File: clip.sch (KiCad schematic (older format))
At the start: 47 parts, among them J1 LiPo, J2 USB_B_Micro, J3 BME680, J4 LIS3DH, J5 Conn_01x07, J6 Conn_01x18, J7 Conn_01x18, Q1 2.5A/30V, Q2 S8050, Q3 S8050, SW1 Switch, SW2 Switch, U1 MCP73831, U2 AP2112K-3.3, U3 FT231XS, U4 ESP32-WROOM-32

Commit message: Rename project
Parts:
- J2: symbol Connector:USB_B_Micro -> clip-rescue:USB_B_Micro-Connector-clip_20200407-rescue
- U2: symbol Regulator_Linear:AP2112K-3.3 -> clip-rescue:AP2112K-3.3-Regulator_Linear-clip_20200407-rescue
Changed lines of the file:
@@
 3.3V
 $Comp
-L Regulator_Linear:AP2112K-3.3 U2
+L clip-rescue:AP2112K-3.3-Regulator_Linear-clip_20200407-rescue U2
 U 1 1 5E773568
 P 2850 1700
@@
 $EndComp
 $Comp
-L Connector:USB_B_Micro J2
+L clip-rescue:USB_B_Micro-Connector-clip_20200407-rescue J2
 U 1 1 5E93C6CC
 P 8000 1800
@@
 Data
 89 50 4E 47 0D 0A 1A 0A 00 00 00 0D 49 48 44 52 00 00 02 EE 00 00 02 1A 08 02 00 00 00 F0 7C 5F
-92 00 00 00 03 73 42 49 54 08 08 08 DB E1 4F E0 00 00 00 09 70 48 59 73 00 00 0E C3 00 00 0E C3
-01 C7 6F A8 64 00 00 20 00 49 44 41 54 78 9C EC BD 77 B4 25 55 99 36 FE BC EF DE BB C2 39 E7 A6
+92 00 00 00 03 73 42 49 54 08 08 08 DB E1 4F E0 00 00 00 09 70 48 59 73 00 00 0E 74 00 00 0E 74
+01 6B 24 B3 D6 00 00 20 00 49 44 41 54 78 9C EC BD 77 B4 25 55 99 36 FE BC EF DE BB C2 39 E7 A6
 EE DB 89 D0 82 C0 88 62 40 07 14 01 85 31 A1 A0 32 E6 08 06 18 31 8E A2 A3 9F A3 A3 23 26 C4 30
 62 D6 31 A0 98 C5 88 A2 A8 33 62 18 B3 62 FA 50 04 15 41 E8 6E BA A1 FB 86 13 AA 6A EF FD BE DF

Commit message: Update design
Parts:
- removed D4: Green, LED_SMD:LED_0805_2012Metric_Pad1.15x1.40mm_HandSolder, symbol Device:LED
- removed J5: Conn_01x07, Connector_PinHeader_2.54mm:PinHeader_1x07_P2.54mm_Vertical, symbol Connector_Generic:Conn_01x07
- removed J6, J7: Conn_01x18, Connector_PinHeader_2.54mm:PinHeader_1x18_P2.54mm_Vertical, symbol Connector_Generic:Conn_01x18
- removed R3: 1K, Resistor_SMD:R_0805_2012Metric_Pad1.15x1.40mm_HandSolder, symbol Device:R_US
- D1: value Red -> Green
- J2: footprint Connector_USB:USB_Micro-B_Amphenol_10103594-0001LF_Horizontal -> Connector_USB:USB_Micro-B_Wuerth_614105150721_Vertical; Digikey 609-4050-1-ND -> 732-5958-1-ND; Digikey_link https://www.digikey.de/product-detail/en/amphenol-icc-fci/1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 -> https://www.digikey.de/product-detail/en/w%C3%BCrth-elektro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; Manufacturer 10103594-0001LF -> 614105150721
- J3: Digikey S7045-ND -> S7006-ND; Digikey_link https://www.digikey.de/product-detail/en/sullins-connector-solutions/PPPC121LFBN-RC/S7045-ND/810184 -> https://www.digikey.de/product-detail/en/sullins-connector-solutions/PPTC081LFBN-RC/S7006-ND/810147; Manufacturer PPPC121LFBN-RC -> PPTC081LFBN-RC
- J4: Digikey 732-5321-ND -> S7006-ND; Digikey_link https://www.digikey.de/product-detail/en/w%C3%BCrth-elektro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 -> https://www.digikey.de/product-detail/en/sullins-connector-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; Manufacturer 61300811121 -> PPTC081LFBN-RC
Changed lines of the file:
@@
 Text Notes 7700 4300 0    39   ~ 0
 Reference: SparkFun_ESP32_thing
-Wire Notes Line
-	4650 550  500  550
 Text Notes 600  650  0    50   ~ 0
 Voltage Regulator and Battery
@@
 Wire Notes Line
 	4700 550  7600 550
-Text Notes 4750 2500 0    39   ~ 0
-Reference: SparkFun_ESP32_Thing_Plus\nCharge current:\nI_CHG = 1000 / R_PROG\nR_PROG=2K : I_CHG=500mA
 Text Notes 4750 650  0    50   ~ 0
 Lithium-Polymer Battery Charger (1-cell)
@@
 P 5800 1050
 F 0 "D1" V 5850 1150 50  0000 L CNN
-F 1 "Red" V 5750 1150 50  0000 L CNN
+F 1 "Green" V 5750 1150 50  0000 L CNN
 F 2 "LED_SMD:LED_0805_2012Metric_Pad1.15x1.40mm_HandSolder" H 5800 1050 50  0001 C CNN
 F 3 "https://katalog.we-online.de/led/datasheet/150080RS75000.pdf" H 5800 1050 50  0001 C CNN
@@
 IO35
 $Comp
-L Connector_Generic:Conn_01x18 J6
+L Connector_Generic:Conn_01x18 #J6
 U 1 1 5E81200B
 P 4150 6400
-F 0 "J6" H 4068 7325 50  0000 C CNN
+F 0 "#J6" H 4068 7325 50  0000 C CNN
 F 1 "Conn_01x18" H 4068 7326 50  0001 C CNN
 F 2 "Connector_PinHeader_2.54mm:PinHeader_1x18_P2.54mm_Vertical" H 4150 6400 50  0001 C CNN
@@
 	5400 5600 5500 5600
 $Comp
-L Connector_Generic:Conn_01x18 J7
+L Connector_Generic:Conn_01x18 #J7
 U 1 1 5E8DE4F0
 P 5200 6400
-F 0 "J7" H 5118 7325 50  0000 C CNN
+F 0 "#J7" H 5118 7325 50  0000 C CNN
 F 1 "Conn_01x18" H 5118 7326 50  0001 C CNN
 F 2 "Connector_PinHeader_2.54mm:PinHeader_1x18_P2.54mm_Vertical" H 5200 6400 50  0001 C CNN
@@
 Reference: NodeMCU_ESP32
 $Comp
-L Device:LED D4
+L Device:LED #D4
 U 1 1 5E75A88B
 P 6050 1950
-F 0 "D4" V 6100 2050 50  0000 L CNN
-F 1 "Green" V 6000 2050 50  0000 L CNN
+F 0 "#D4" V 6100 2050 50  0000 L CNN
+F 1 "Red" V 6000 2050 50  0000 L CNN
 F 2 "LED_SMD:LED_0805_2012Metric_Pad1.15x1.40mm_HandSolder" H 6050 1950 50  0001 C CNN
 F 3 "https://katalog.we-online.de/led/datasheet/150080GS75000.pdf" H 6050 1950 50  0001 C CNN
@@
 $EndComp
 $Comp
-L Device:R_US R3
+L Device:R_US #R3
 U 1 1 5E759248
 P 6050 1650
-F 0 "R3" H 5850 1600 50  0000 L CNN
+F 0 "#R3" H 5850 1600 50  0000 L CNN
 F 1 "1K" H 5900 1700 50  0000 L CNN
 F 2 "Resistor_SMD:R_0805_2012Metric_Pad1.15x1.40mm_HandSolder" V 6090 1640 50  0001 C CNN
@@
 	10500 5200 10850 5200
 $Comp
-L Connector_Generic:Conn_01x07 J5
+L Connector_Generic:Conn_01x07 #J5
 U 1 1 5E79B981
 P 6250 5900
-F 0 "J5" H 6330 5942 50  0000 L CNN
+F 0 "#J5" H 6330 5942 50  0000 L CNN
 F 1 "Conn_01x07" H 6330 5851 50  0001 L CNN
 F 2 "Connector_PinHeader_2.54mm:PinHeader_1x07_P2.54mm_Vertical" H 6250 5900 50  0001 C CNN
@@
 	1    0    0    -1
 $EndComp
-Text Notes 2700 1250 0    39   ~ 0
+Text Notes 2500 1250 0    39   ~ 0
 AP2112K/AMS1117-3.3\n
 Text Notes 1500 1150 0    39   ~ 0
@@
 Text Notes 850  1900 0    39   ~ 0
 BAT20J/S4-1N5819/SS14\n
-Text Notes 600  2500 0    39   ~ 0
-Reference: SparkFun_ESP32_Thing_Plus\nVBUS - 6V MAX\nBATT - Single Cell (4.2V MAX)
 Wire Wire Line
 	1850 1600 2300 1600
@@
 Wire Wire Line
 	8700 3100 8700 3000
-Connection ~ 8700 3100
 Wire Wire Line
 	8450 3100 8700 3100
-Wire Wire Line
-	8450 3150 8450 3100
-$Comp
-L Device:C_Small C9
-U 1 1 5EAF9B4F
-P 8700 3250
-F 0 "C9" H 8792 3296 50  0000 L CNN
-F 1 "4.7uF/6.3V" H 8792 3205 50  0000 L CNN
-F 2 "Capacitor_SMD:C_0805_2012Metric_Pad1.15x1.40mm_HandSolder" H 8700 3250 50  0001 C CNN
-F 3 "https://katalog.we-online.de/pbs/datasheet/885012207002.pdf" H 8700 3250 50  0001 C CNN
-F 4 "732-7647-1-ND" H 8700 3250 50  0001 C CNN "Digikey"
-F 5 "https://www.digikey.com/product-detail/en/w%C3%BCrth-elektronik/885012207002/732-7647-1-ND/5454274" H 8700 3250 50  0001 C CNN "Digikey_link"
-F 6 "885012207002" H 8700 3250 50  0001 C CNN "Manufacturer"
-	1    8700 3250
-	1    0    0    -1
-$EndComp
-Wire Wire Line
-	8700 3350 8700 3500
 $Comp
 L Device:R_US R7
@@
 Wire Wire Line
 	8700 3500 8700 3600
-Connection ~ 8700 3500
 Wire Wire Line
 	8450 3500 8700 3500
-Wire Wire Line
-	8450 3350 8450 3500
-$Comp
-L Device:C_Small C8
-U 1 1 5EB20E1C
-P 8450 3250
-F 0 "C8" H 8250 3300 50  0000 L CNN
-F 1 "0.1uF/50V" H 7950 3200 50  0000 L CNN
-F 2 "Capacitor_SMD:C_0805_2012Metric_Pad1.15x1.40mm_HandSolder" H 8450 3250 50  0001 C CNN
-F 3 "https://katalog.we-online.de/pbs/datasheet/885012207098.pdf" H 8450 3250 50  0001 C CNN
-F 4 "732-8080-1-ND" H 8450 3250 50  0001 C CNN "Digikey"
-F 5 "https://www.digikey.de/product-detail/en/w%C3%BCrth-elektronik/885012207098/732-8080-1-ND/5454707" H 8450 3250 50  0001 C CNN "Digikey_link"
-F 6 "885012207098" H 8450 3250 50  0001 C CNN "Manufacturer"
-	1    8450 3250
-	1    0    0    -1
-$EndComp
 $Comp
 L power:GND #PWR028
@@
 	1    0    0    -1
 $EndComp
-Wire Wire Line
-	8700 3150 8700 3100
 $Comp
 L power:VBUS #PWR023
@@
 F 0 "J2" H 8057 2267 50  0000 C CNN
 F 1 "USB_B_Micro" H 8057 2176 50  0000 C CNN
-F 2 "Connector_USB:USB_Micro-B_Amphenol_10103594-0001LF_Horizontal" H 8150 1750 50  0001 C CNN
-F 3 "https://cdn.amphenol-icc.com/media/wysiwyg/files/drawing/10103594.pdf" H 8150 1750 50  0001 C CNN
-F 4 "609-4050-1-ND" H 8000 1800 50  0001 C CNN "Digikey"
-F 5 "https://www.digikey.de/product-detail/en/amphenol-icc-fci/10103594-0001LF/609-4050-2-ND/2350351" H 8000 1800 50  0001 C CNN "Digikey_link"
-F 6 "10103594-0001LF" H 8000 1800 50  0001 C CNN "Manufacturer"
+F 2 "Connector_USB:USB_Micro-B_Wuerth_614105150721_Vertical" H 8150 1750 50  0001 C CNN
+F 3 "https://www.we-online.de/katalog/datasheet/614105150721.pdf" H 8150 1750 50  0001 C CNN
+F 4 "732-5958-1-ND" H 8000 1800 50  0001 C CNN "Digikey"
+F 5 "https://www.digikey.de/product-detail/en/w%C3%BCrth-elektronik/614105150721/732-5958-1-ND/5047553" H 8000 1800 50  0001 C CNN "Digikey_link"
+F 6 "614105150721" H 8000 1800 50  0001 C CNN "Manufacturer"
 	1    8000 1800
 	1    0    0    -1
@@
 F 2 "Connector_PinHeader_2.54mm:PinHeader_1x07_P2.54mm_Vertical" H 4950 3850 50  0001 C CNN
 F 3 "https://media.digikey.com/pdf/Data%20Sheets/Sullins%20PDFs/Female_Headers.100_DS.pdf" H 4950 3850 50  0001 C CNN
-F 4 "S7045-ND" H 4950 3850 50  0001 C CNN "Digikey"
-F 5 "https://www.digikey.de/product-detail/en/sullins-connector-solutions/PPPC121LFBN-RC/S7045-ND/810184" H 4950 3850 50  0001 C CNN "Digikey_link"
-F 6 "PPPC121LFBN-RC" H 4950 3850 50  0001 C CNN "Manufacturer"
+F 4 "S7006-ND" H 4950 3850 50  0001 C CNN "Digikey"
+F 5 "https://www.digikey.de/product-detail/en/sullins-connector-solutions/PPTC081LFBN-RC/S7006-ND/810147" H 4950 3850 50  0001 C CNN "Digikey_link"
+F 6 "PPTC081LFBN-RC" H 4950 3850 50  0001 C CNN "Manufacturer"
 	1    4950 3850
 	1    0    0    -1
@@
 F 1 "LIS3DH" H 6730 3751 50  0000 L CNN
 F 2 "Connector_PinHeader_2.54mm:PinHeader_1x08_P2.54mm_Vertical" H 6650 3850 50  0001 C CNN
-F 3 "https://katalog.we-online.de/em/datasheet/6130xx11121.pdf" H 6650 3850 50  0001 C CNN
-F 4 "732-5321-ND" H 6650 3850 50  0001 C CNN "Digikey"
-F 5 "https://www.digikey.de/product-detail/en/w%C3%BCrth-elektronik/61300811121/732-5321-ND/4846839" H 6650 3850 50  0001 C CNN "Digikey_link"
-F 6 "61300811121" H 6650 3850 50  0001 C CNN "Manufacturer"
+F 3 "https://media.digikey.com/pdf/Data%20Sheets/Sullins%20PDFs/Female_Headers.100_DS.pdf" H 6650 3850 50  0001 C CNN
+F 4 "S7006-ND" H 6650 3850 50  0001 C CNN "Digikey"
+F 5 "https://www.digikey.de/product-detail/en/sullins-connector-solutions/PPTC081LFBN-RC/S7006-ND/810147" H 6650 3850 50  0001 C CNN "Digikey_link"
+F 6 "PPTC081LFBN-RC" H 6650 3850 50  0001 C CNN "Manufacturer"
 	1    6650 3850
 	1    0    0    -1
@@
 EndData
 $EndBitmap
+Connection ~ 8700 3500
+Connection ~ 8700 3100
+Wire Wire Line
+	8700 3150 8700 3100
+$Comp
+L Device:C_Small C8
+U 1 1 5EB20E1C
+P 8450 3250
+F 0 "C8" H 8250 3300 50  0000 L CNN
+F 1 "0.1uF/50V" H 7950 3200 50  0000 L CNN
+F 2 "Capacitor_SMD:C_0805_2012Metric_Pad1.15x1.40mm_HandSolder" H 8450 3250 50  0001 C CNN
+F 3 "https://katalog.we-online.de/pbs/datasheet/885012207098.pdf" H 8450 3250 50  0001 C CNN
+F 4 "732-8080-1-ND" H 8450 3250 50  0001 C CNN "Digikey"
+F 5 "https://www.digikey.de/product-detail/en/w%C3%BCrth-elektronik/885012207098/732-8080-1-ND/5454707" H 8450 3250 50  0001 C CNN "Digikey_link"
+F 6 "885012207098" H 8450 3250 50  0001 C CNN "Manufacturer"
+	1    8450 3250
+	1    0    0    -1
+$EndComp
+Wire Wire Line
+	8450 3350 8450 3500
+Wire Wire Line
+	8700 3350 8700 3500
+$Comp
+L Device:C_Small C9
+U 1 1 5EAF9B4F
+P 8700 3250
+F 0 "C9" H 8792 3296 50  0000 L CNN
+F 1 "4.7uF/6.3V" H 8792 3205 50  0000 L CNN
+F 2 "Capacitor_SMD:C_0805_2012Metric_Pad1.15x1.40mm_HandSolder" H 8700 3250 50  0001 C CNN
+F 3 "https://katalog.we-online.de/pbs/datasheet/885012207002.pdf" H 8700 3250 50  0001 C CNN
+F 4 "732-7647-1-ND" H 8700 3250 50  0001 C CNN "Digikey"
+F 5 "https://www.digikey.com/product-detail/en/w%C3%BCrth-elektronik/885012207002/732-7647-1-ND/5454274" H 8700 3250 50  0001 C CNN "Digikey_link"
+F 6 "885012207002" H 8700 3250 50  0001 C CNN "Manufacturer"
+	1    8700 3250
+	1    0    0    -1
+$EndComp
+Wire Wire Line
+	8450 3150 8450 3100
+Text Notes 4750 2500 0    39   ~ 0
+Reference: SparkFun_ESP32_Thing_Plus\nCharge current:\nI_CHG = 1000 / R_PROG\nR_PROG=2K : I_CHG=500mA
+Text Notes 600  2500 0    39   ~ 0
+Reference: SparkFun_ESP32_Thing_Plus\nVBUS - 6V MAX\nBATT - Single Cell (4.2V MAX)
+Wire Notes Line
+	4650 550  550  550
 $EndSCHEMATC

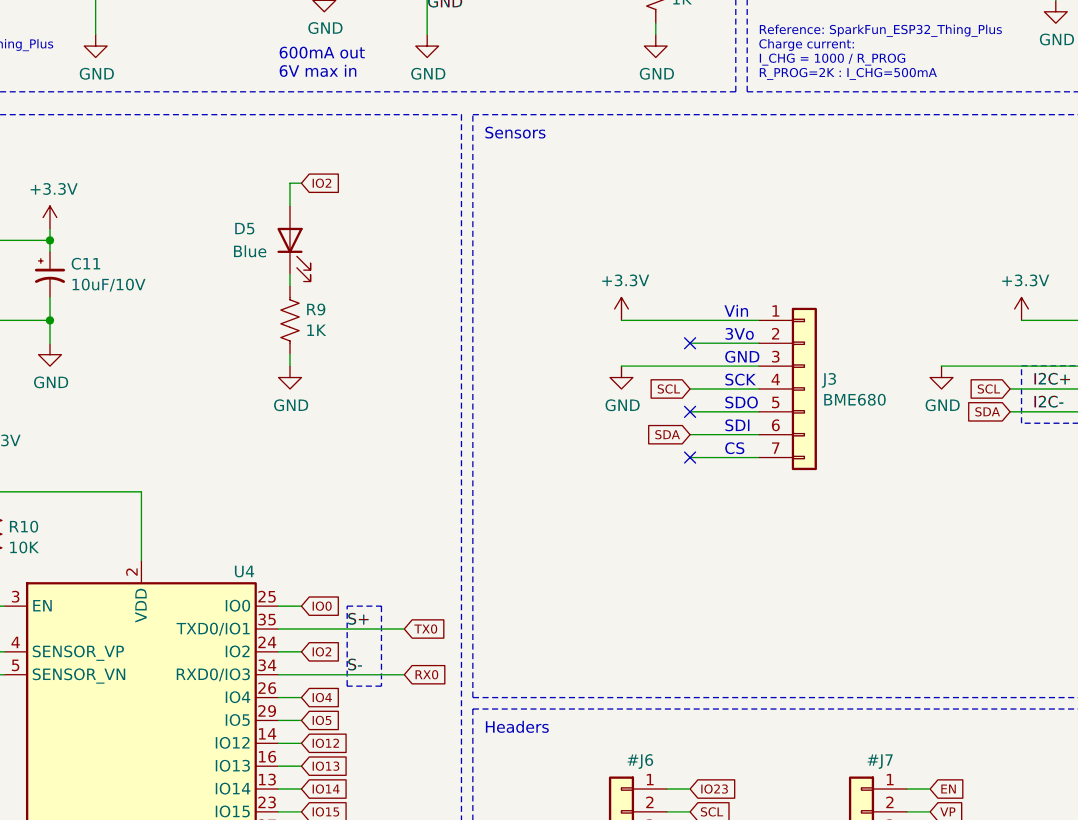
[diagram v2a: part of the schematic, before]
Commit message: Add Moisture Sensor Header
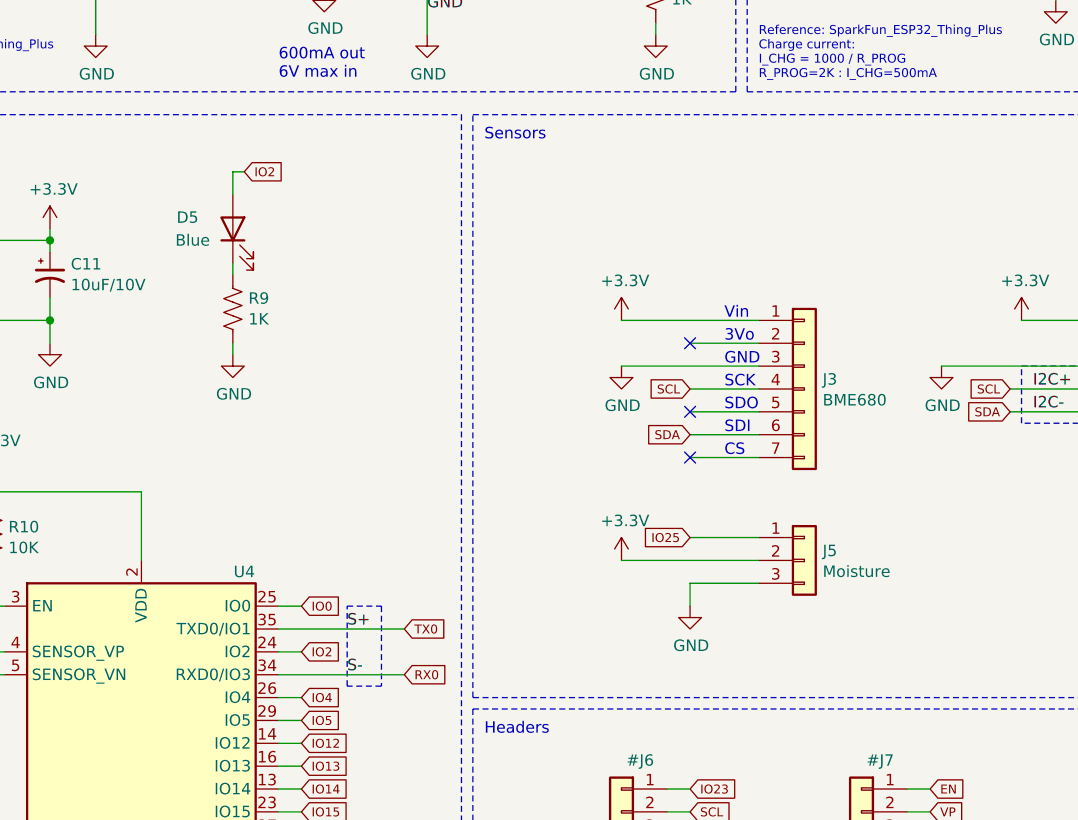
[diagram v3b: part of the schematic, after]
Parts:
- added J5: Moisture, symbol Connector_Generic:Conn_01x03
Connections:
- net +3V3: now also J5.2 (Pin_2)
- net GND: now also J5.3 (Pin_3)
- net IO25: now also J5.1 (Pin_1)
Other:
- moved on the sheet: D5, R9

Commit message: Refactor design
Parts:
- J2: footprint Connector_USB:USB_Micro-B_Wuerth_614105150721_Vertical -> Connector_USB:USB_Micro-B_Wuerth_629105150521; Digikey 732-5958-1-ND -> 732-5960-1-ND; Digikey_link https://www.digikey.de/product-detail/en/w%C3%BCrth-elektro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 -> https://www.digikey.de/product-detail/de/w%C3%BCrth-elektro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
- J5: footprint (none) -> Connector_PinHeader_2.54mm:PinHeader_1x03_P2.54mm_Horizontal
- JP1: footprint Connector_PinHeader_2.54mm:PinHeader_1x02_P2.54mm_Vertical -> Jumper:SolderJumper-2_P1.3mm_Open_TrianglePad1.0x1.5mm
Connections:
- net IO25: no longer J5.1 (Pin_1)
- net IO34: now also J5.1 (Pin_1)
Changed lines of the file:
@@
 F 0 "JP1" H 3900 1805 50  0000 C CNN
 F 1 "SJ" H 3900 1714 50  0000 C CNN
-F 2 "Connector_PinHeader_2.54mm:PinHeader_1x02_P2.54mm_Vertical" H 3900 1600 50  0001 C CNN
+F 2 "Jumper:SolderJumper-2_P1.3mm_Open_TrianglePad1.0x1.5mm" H 3900 1600 50  0001 C CNN
 F 3 "https://katalog.we-online.de/em/datasheet/6130xx11121.pdf" H 3900 1600 50  0001 C CNN
 F 4 "https://www.digikey.de/product-detail/en/w%C3%BCrth-elektronik/61301811121/732-5328-ND/4846858" H 3900 1600 50  0001 C CNN "Digikey_link"
@@
 F 0 "J2" H 8057 2267 50  0000 C CNN
 F 1 "USB_B_Micro" H 8057 2176 50  0000 C CNN
-F 2 "Connector_USB:USB_Micro-B_Wuerth_614105150721_Vertical" H 8150 1750 50  0001 C CNN
-F 3 "https://www.we-online.de/katalog/datasheet/614105150721.pdf" H 8150 1750 50  0001 C CNN
-F 4 "732-5958-1-ND" H 8000 1800 50  0001 C CNN "Digikey"
-F 5 "https://www.digikey.de/product-detail/en/w%C3%BCrth-elektronik/614105150721/732-5958-1-ND/5047553" H 8000 1800 50  0001 C CNN "Digikey_link"
+F 2 "Connector_USB:USB_Micro-B_Wuerth_629105150521" H 8150 1750 50  0001 C CNN
+F 3 "https://www.we-online.de/katalog/datasheet/629105150521.pdf" H 8150 1750 50  0001 C CNN
+F 4 "732-5960-1-ND" H 8000 1800 50  0001 C CNN "Digikey"
+F 5 "https://www.digikey.de/product-detail/de/w%C3%BCrth-elektronik/629105150521/732-5960-1-ND/5047555" H 8000 1800 50  0001 C CNN "Digikey_link"
 F 6 "614105150721" H 8000 1800 50  0001 C CNN "Manufacturer"
 	1    8000 1800
@@
 F 0 "J5" H 5030 4642 50  0000 L CNN
 F 1 "Moisture" H 5030 4551 50  0000 L CNN
-F 2 "" H 4950 4600 50  0001 C CNN
+F 2 "Connector_PinHeader_2.54mm:PinHeader_1x03_P2.54mm_Horizontal" H 4950 4600 50  0001 C CNN
 F 3 "~" H 4950 4600 50  0001 C CNN
 	1    4950 4600
@@
 $EndBitmap
 Text GLabel 4450 4500 0    39   Input ~ 0
-IO25
+IO34
 Wire Wire Line
 	4750 4500 4450 4500

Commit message: Update design
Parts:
- removed C5, C6: 47pF/16V, Capacitor_SMD:C_0805_2012Metric_Pad1.15x1.40mm_HandSolder, symbol Device:C_Small
- removed C7, C8: 0.1uF/50V, Capacitor_SMD:C_0805_2012Metric_Pad1.15x1.40mm_HandSolder, symbol Device:C_Small
- removed C9: 4.7uF/6.3V, Capacitor_SMD:C_0805_2012Metric_Pad1.15x1.40mm_HandSolder, symbol Device:C_Small
- removed Q2, Q3: S8050, Package_TO_SOT_SMD:SOT-23, symbol Transistor_BJT:S8050
- removed R12, R13: 10K, Resistor_SMD:R_0805_2012Metric_Pad1.15x1.40mm_HandSolder, symbol Device:R_US
- removed R4, R7: 27, Resistor_SMD:R_0805_2012Metric_Pad1.15x1.40mm_HandSolder, symbol Device:R_US
- removed U3: FT231XS, Package_SO:SSOP-20_3.9x8.7mm_P0.635mm, symbol Interface_USB:FT231XS
- added D4: Green, LED_SMD:LED_0805_2012Metric_Pad1.15x1.40mm_HandSolder, symbol Device:LED
- added J6: Conn_01x07, Connector_PinHeader_2.54mm:PinHeader_1x06_P2.54mm_Vertical, symbol Connector_Generic:Conn_01x06
- added J7, J8: Conn_01x07, Connector_PinHeader_2.54mm:PinHeader_1x02_P2.54mm_Vertical, symbol Connector_Generic:Conn_01x02
- added R3: 1K, Resistor_SMD:R_0805_2012Metric_Pad1.15x1.40mm_HandSolder, symbol Device:R_US
- D1: value Green -> Red
- J2: footprint Connector_USB:USB_Micro-B_Wuerth_629105150521 -> Connector_USB:USB_Micro-B_Wuerth_614105150721_Vertical
- renumbered C10 to C5, C11 to C6, C12 to C7, R5 to R4, R6 to R5, R8 to R6, R11 to R7, R9 to R8, R10 to R9, U4 to U3
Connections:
- net +3V3: now also J6.6 (Pin_6), J8.2 (Pin_2); no longer C5.1, C6.1, U3.2 (VDD)
- net +BATT: now also J1.1 (Pin_1); no longer J1.2 (Pin_2)
- net EN: now also J6.3 (Pin_3)
- net GND: now also J1.2 (Pin_2), D4.1 (K), J6.1 (Pin_1), J7.2 (Pin_2); no longer J1.1 (Pin_1)
- net IO0: now also J6.2 (Pin_2)
- net RX0: now also J6.4 (Pin_4)
- net TX0: now also J6.5 (Pin_5)
- net VBUS: now also J7.1 (Pin_1)
- net at R1.1, U1.1 (STAT): now also R3.2
- net D+: no longer names the net of J2.3 (D+)
- net D-: no longer names the net of J2.2 (D-)
- new net: C5.1, C6.1, J8.1 (Pin_1), U3.2 (VDD)
- new net: D4.2 (A), R3.1
- no-connect marks 16 -> 11
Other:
- note added: "Ref: https://docs.m5stack.com/en/tool/usb_downloader?id=schematic"
- note added: "Reference: SparkFun_ESP32_Thing_Plus/Adafruit MicroLipo\nCharge current:\nI_CHG = 1000 / R_PROG\nR_PROG=2K : I_CHG=500mA"
- note added: "USB-To-TTL"
- note removed: "Auto-Reset"
- note removed: "Reference: SparkFun_ESP32_Thing_Plus\nCharge current:\nI_CHG = 1000 / R_PROG\nR_PROG=2K : I_CHG=500mA"
- note removed: "Reference: SparkFun_ESP32_thing"
- note removed: "USB-to-Serial-Module"
- moved on the sheet: C1, C2, C3, C4, C5, C6, C7, D1, D2, D3, D5, J1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

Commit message: Update design
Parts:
- added J6: Conn_01x07, Connector_PinHeader_2.54mm:PinHeader_1x02_P2.54mm_Vertical, symbol Connector_Generic:Conn_01x02
- renumbered J1 to BATTERY1, C5 to C2, C6 to C3, C2 to C4, C3 to C5, C4 to C6, D4 to D2, D5 to D3, D2 to D4, D3 to D5, J8 to J1, J3 to J2, J5 to J3, J7 to J4, J4 to J5, J2 to J7, J6 to J8, R9 to R1, R1 to R2, R5 to R4, R8 to R5, R2 to R6, R4 to R7, R6 to R8, R7 to R9, U3 to U1, U1 to U2, U2 to U3
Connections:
- net GND: now also J6.1 (Pin_1)
- net IO0: now also J6.2 (Pin_2)
- no-connect marks 11 -> 10
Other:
- moved on the sheet: C7, J2, J3, J5, SW2
